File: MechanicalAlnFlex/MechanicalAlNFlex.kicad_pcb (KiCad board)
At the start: 2 copper layers, 41.5 x 15 mm, 10 parts, among them J3 FTE-130-01-G-DV-EC

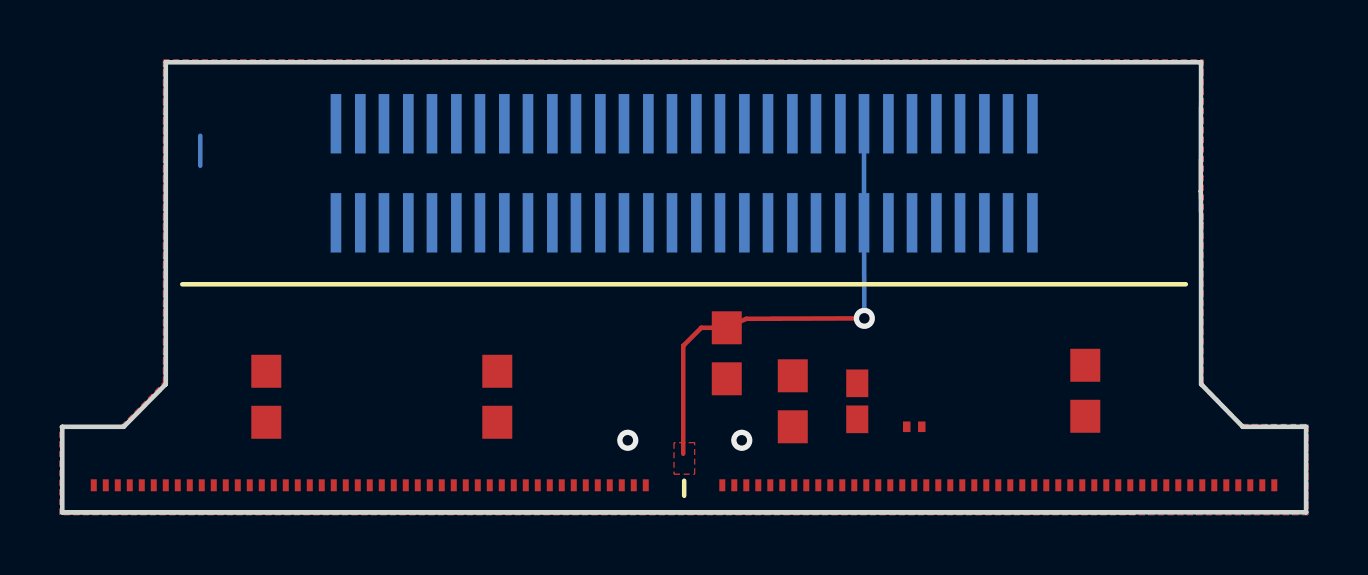
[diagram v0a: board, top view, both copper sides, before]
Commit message: Updates MechanicalAlnFlex for new pad number and dimensions
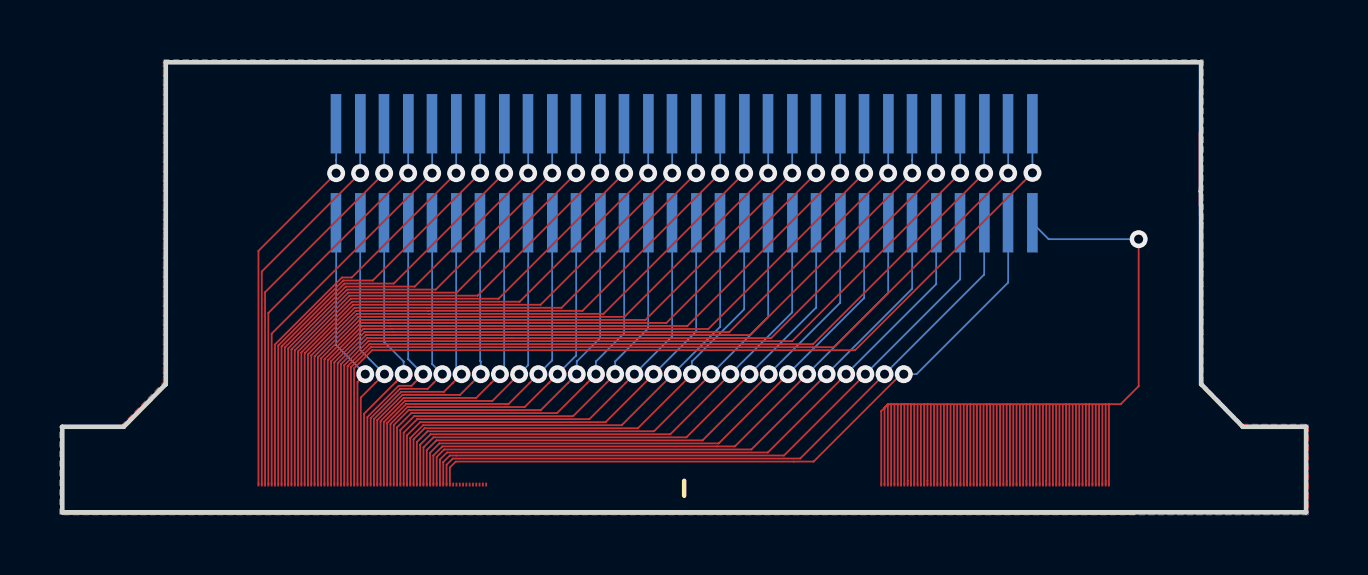
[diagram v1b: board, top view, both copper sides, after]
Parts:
- removed C1, C2, C4, C5, C6: C-USC0603, MechanicalAlNFlex:C0603
- removed C7: C-USC0402K, MechanicalAlNFlex:C0402K
- removed C8: C-USC0201, MechanicalAlNFlex:C0201
- removed ETROC1, ETROC2: ETROC, MechanicalAlNFlex:ETROC
- added J2: Conn_02x35_Top_Bottom, unl_silab:ETROC_70pad_61x126um_110um_pitch, F.Cu at (134.3, 111.6)
- added J3: Conn_02x35_Top_Bottom, unl_silab:ETROC_70pad_61x126um_110um_pitch, F.Cu at (155.1, 111.6)
- J1: renamed from J3; value FTE-130-01-G-DV-EC -> Conn_02x30_Odd_Even
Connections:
- J1 pad 1: /GND -> /COM
- J1 pad 10: Net-(J3-Pad10) -> /P26
- J1 pad 11: /GND -> /P55
- J1 pad 12: /GND -> /P25
- J1 pad 13: Net-(J3-Pad13) -> /P54
- J1 pad 14: Net-(J3-Pad14) -> /P24
- J1 pad 15: /VBIAS -> /P53
- J1 pad 16: /VBIAS -> /P23
- J1 pad 17: Net-(J3-Pad17) -> /P52
- J1 pad 18: Net-(J3-Pad18) -> /P22
- J1 pad 19: /GND -> /P51
- J1 pad 2: /GND -> /P30
- J1 pad 20: /GND -> /P21
- J1 pad 21: Net-(J3-Pad21) -> /P50
- J1 pad 22: Net-(J3-Pad22) -> /P20
- J1 pad 23: Net-(J3-Pad23) -> /P49
- J1 pad 24: Net-(J3-Pad24) -> /P19
- J1 pad 25: Net-(J3-Pad25) -> /P48
- J1 pad 26: Net-(J3-Pad26) -> /P18
- J1 pad 27: Net-(J3-Pad27) -> /P47
- J1 pad 28: Net-(J3-Pad28) -> /P17
- J1 pad 29: Net-(J3-Pad29) -> /P46
- J1 pad 3: Net-(J3-Pad3) -> /P59
- J1 pad 30: Net-(J3-Pad30) -> /P16
- J1 pad 31: (no net) -> /P45
- J1 pad 32: (no net) -> /P15
- J1 pad 33: (no net) -> /P44
- J1 pad 34: (no net) -> /P14
- J1 pad 35: (no net) -> /P43
- J1 pad 36: (no net) -> /P13
- J1 pad 37: (no net) -> /P42
- J1 pad 38: (no net) -> /P12
- J1 pad 39: (no net) -> /P41
- J1 pad 4: Net-(J3-Pad4) -> /P29
- J1 pad 40: (no net) -> /P11
- J1 pad 41: (no net) -> /P40
- J1 pad 42: (no net) -> /P10
- J1 pad 43: (no net) -> /P39
- J1 pad 44: (no net) -> /P9
- J1 pad 45: (no net) -> /P38
- J1 pad 46: (no net) -> /P8
- J1 pad 47: (no net) -> /P37
- J1 pad 48: (no net) -> /P7
- J1 pad 49: (no net) -> /P36
- J1 pad 5: Net-(J3-Pad5) -> /P58
- J1 pad 50: (no net) -> /P6
- J1 pad 51: (no net) -> /P35
- J1 pad 52: (no net) -> /P5
- J1 pad 53: (no net) -> /P34
- J1 pad 54: (no net) -> /P4
- J1 pad 55: (no net) -> /P33
- J1 pad 56: (no net) -> /P3
- J1 pad 57: (no net) -> /P32
- J1 pad 58: (no net) -> /P2
- J1 pad 59: (no net) -> /P31
- J1 pad 6: Net-(J3-Pad6) -> /P28
- J1 pad 60: (no net) -> /P1
- J1 pad 7: Net-(J3-Pad7) -> /P57
- J1 pad 8: Net-(J3-Pad8) -> /P27
- J1 pad 9: Net-(J3-Pad9) -> /P56
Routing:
- net /COM: track 0.00 -> 204.5 mm, vias 0 -> 1
- net /P30: track 0.00 -> 30.8 mm, vias 0 -> 1
- net /P29: track 0.00 -> 30.2 mm, vias 0 -> 1
- net /P28: track 0.00 -> 29.5 mm, vias 0 -> 1
- net /P27: track 0.00 -> 28.8 mm, vias 0 -> 1
- net /P26: track 0.00 -> 28.1 mm, vias 0 -> 1
- net /P25: track 0.00 -> 27.5 mm, vias 0 -> 1
- net /P24: track 0.00 -> 26.7 mm, vias 0 -> 1
- net /P23: track 0.00 -> 26.1 mm, vias 0 -> 1
- net /P22: track 0.00 -> 25.5 mm, vias 0 -> 1
- net /P21: track 0.00 -> 24.8 mm, vias 0 -> 1
- net /P20: track 0.00 -> 24.1 mm, vias 0 -> 1
- net /P59: track 0.00 -> 23.7 mm, vias 0 -> 1
- net /P19: track 0.00 -> 23.4 mm, vias 0 -> 1
- net /P58: track 0.00 -> 22.9 mm, vias 0 -> 1
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- removed copper zone on F.Cu, net (none)
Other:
- net class Default: clearance 0.1524 -> 0.04; trace_width 0.25 -> 0.061; via_dia 0.8 -> 0.6; via_drill 0.4 -> 0.3
- rule trace_clearance: 0.1524 -> 0.04
- rule trace_min: 0.1524 -> 0.05
- rule via_min_drill: 0.3 -> 0.2
- rule via_min_size: 0.4 -> 0.5

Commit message: Misc updates
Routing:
- added copper zone on B.Cu, net (none)
- added copper zone on F.Cu, net (none)
- removed copper zone on B.Cu, net /GND
- removed copper zone on F.Cu, net /GND
